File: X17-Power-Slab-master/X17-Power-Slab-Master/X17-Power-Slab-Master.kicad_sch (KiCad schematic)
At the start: 18 parts, among them J2 ET60T-D04-3-08-D04-X-R1-S, J3 796636-6, Q2 IRF1018ESTRLPBF, U1 AZ1117IH-3.3TRG1

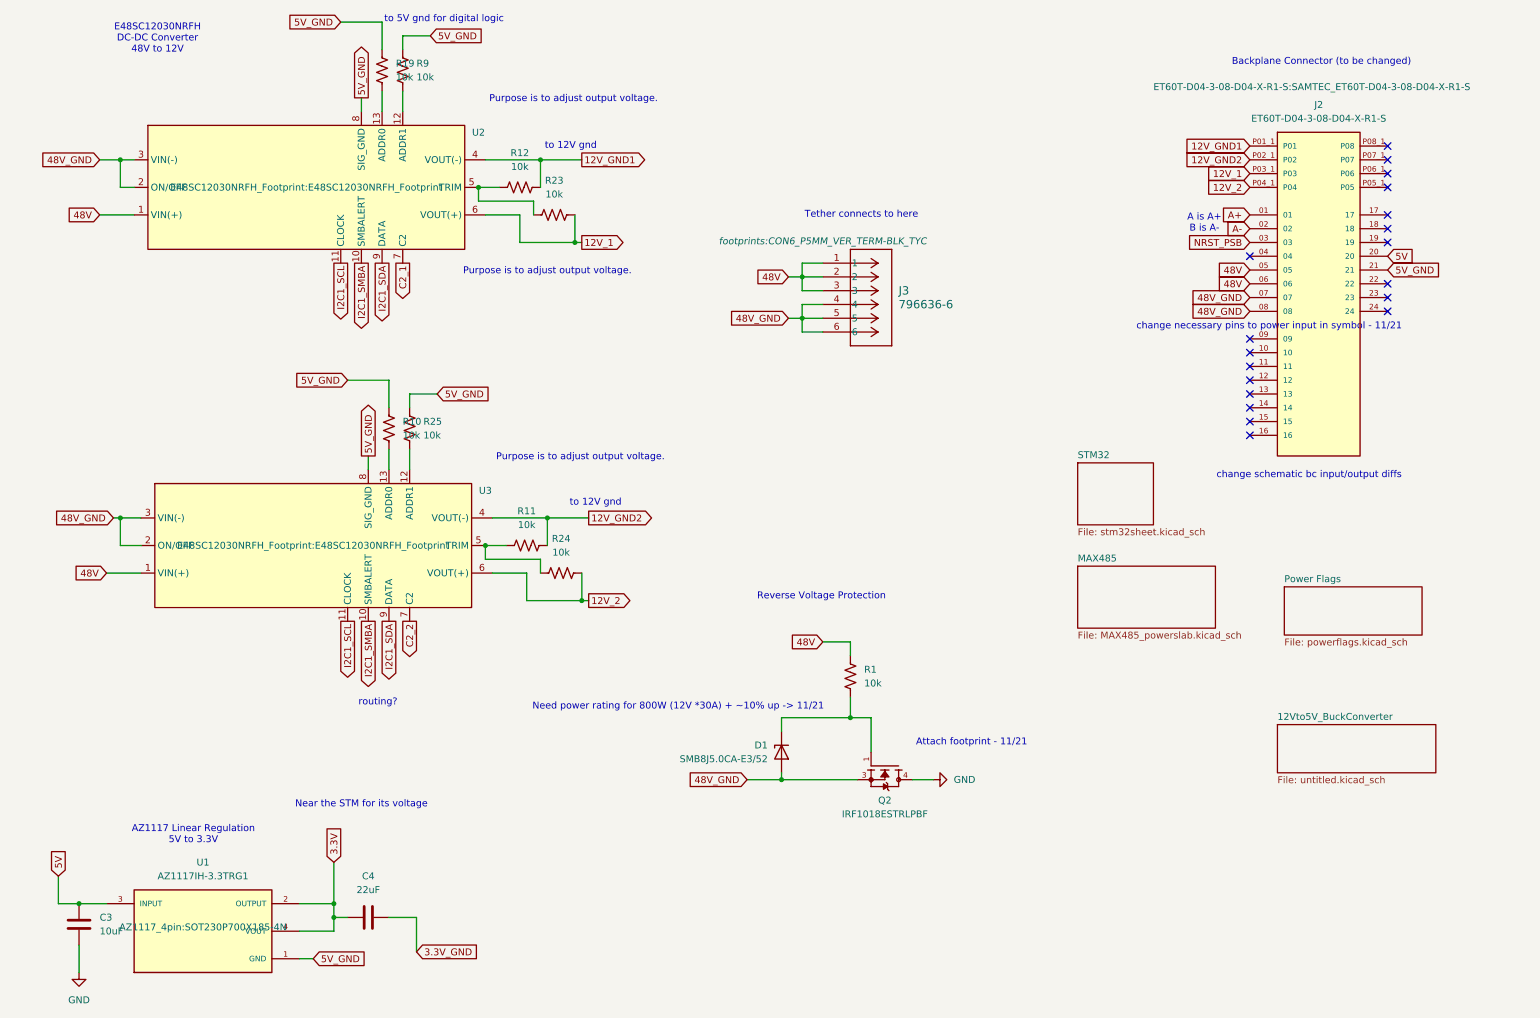
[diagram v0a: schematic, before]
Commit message: Routes
Cannot fill the polygons for some reason
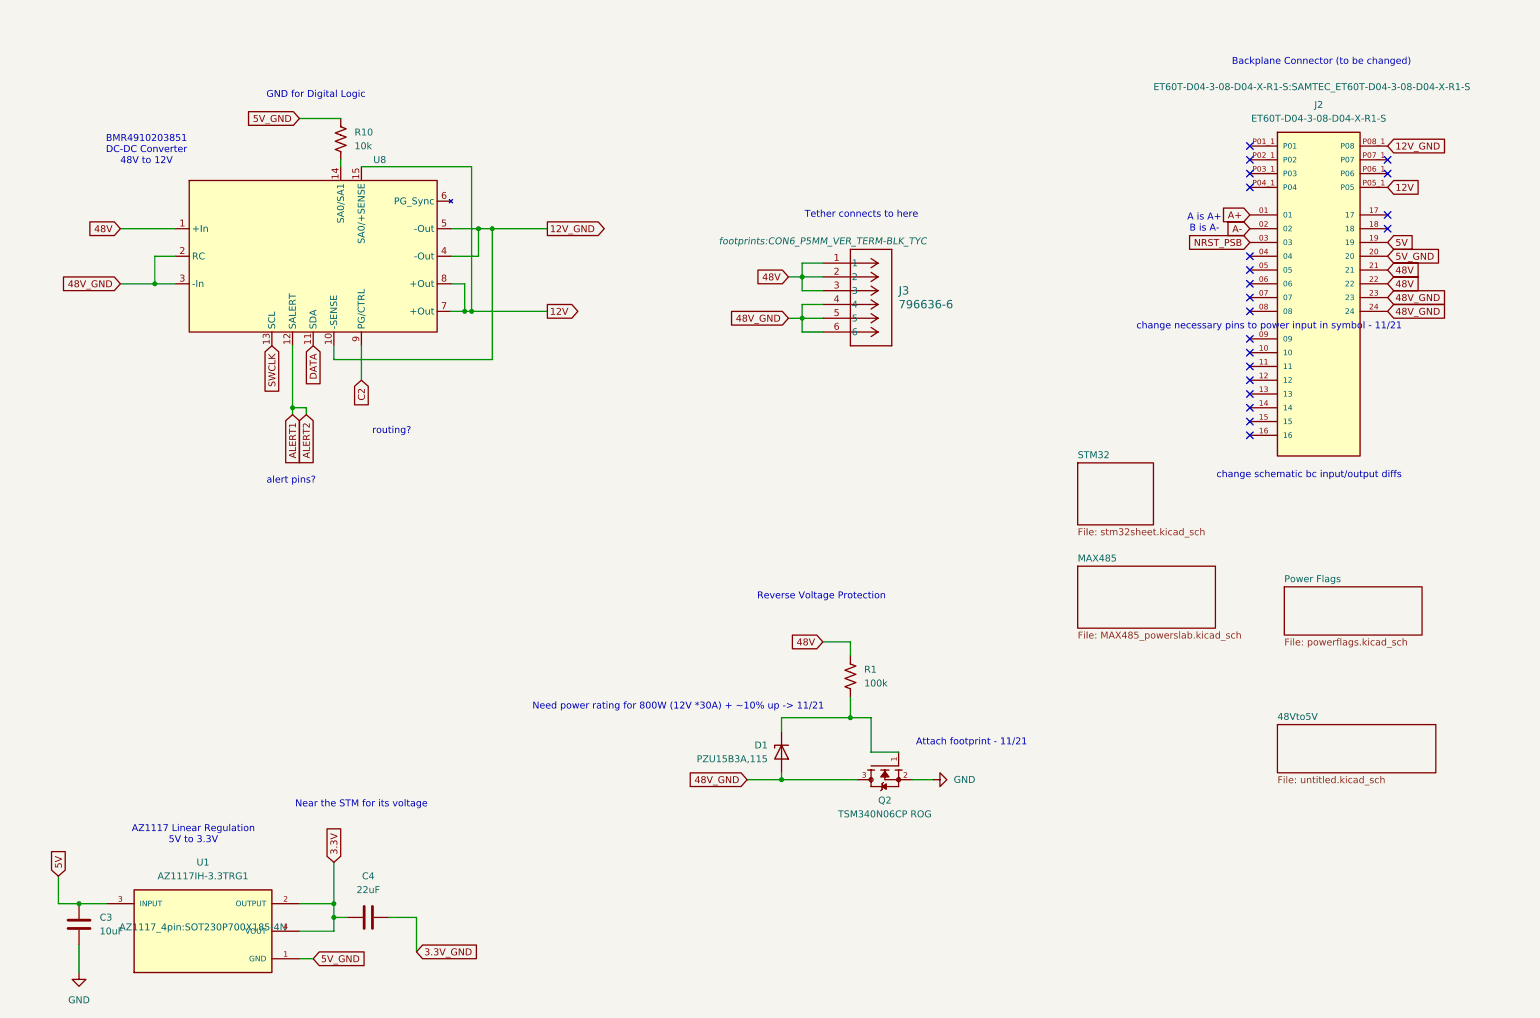
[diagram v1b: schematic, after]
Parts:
- removed R11, R12, R19, R23, R24, R25, R9: 10k, Resistor_SMD:R_0603_1608Metric_Pad0.98x0.95mm_HandSolder, symbol Device:R_US
- removed U2, U3: ~, E48SC12030NRFH_Footprint:E48SC12030NRFH_Footprint, symbol E48SC12030NRFH_New:E48SC12030NRFH
- added U8: ~, BMR491_MadeByMe:BMR4910203851, symbol BMR491_SymbolByMe:BMR4910203/851
- D1: value SMB8J5.0CA-E3/52 -> PZU15B3A,115
- Q2: value IRF1018ESTRLPBF -> TSM340N06CP ROG; footprint Reverse Voltage Protection:TO254P1524X483-4 -> Reverse Voltage Protection:TRANS_TSM340N06CPROG; MANUFACTURER Infineon -> TSM
- R1: value 10k -> 100k
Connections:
- net 48V: now also J2.21, J2.22, U8.1 (+In); no longer J2.05, J2.06
- net 48V_GND: now also J2.23, J2.24, U8.2 (RC), U8.3 (-In); no longer J2.07, J2.08
- net 5V: now also J2.19; no longer J2.20
- net 5V_GND: now also J2.20; no longer J2.21
- net GND: now also Q2.2; no longer Q2.4
- net at R10.2: now also U8.14 (SA0/SA1)
- net 12V: now reaches J2.P05_1 (P05)
- net 12V: now also U8.15 (SA0/+SENSE), U8.7 (+Out), U8.8 (+Out)
- net 12V_GND: now reaches J2.P08_1 (P08)
- net 12V_GND: now also U8.10 (-SENSE), U8.4 (-Out), U8.5 (-Out)
- net 12V_1: no longer names the net of J2.P03_1 (P03)
- net 12V_2: no longer names the net of J2.P04_1 (P04)
- net 12V_GND1: no longer names the net of J2.P01_1 (P01)
- net 12V_GND2: no longer names the net of J2.P02_1 (P02)
- new net ALERT1: U8.12 (SALERT)
- new net C2: U8.9 (PG/CTRL)
- new net DATA: U8.11 (SDA)
- new net SWCLK: U8.13 (SCL)
- no-connect marks 19 -> 21
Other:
- sheet 12Vto5V_BuckConverter renamed 48Vto5V
- note added: "BMR4910203851 DC-DC Converter 48V to 12V"
- note added: "GND for Digital Logic"
- note added: "alert pins?"
- note removed: "E48SC12030NRFH DC-DC Converter 48V to 12V"
- note removed: "Purpose is to adjust output voltage."
- note removed: "to 12V gnd"
- note removed: "to 5V gnd for digital logic"
- moved on the sheet: Q2

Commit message: Power traces update
I think I'm getting the idea of power traces needed?
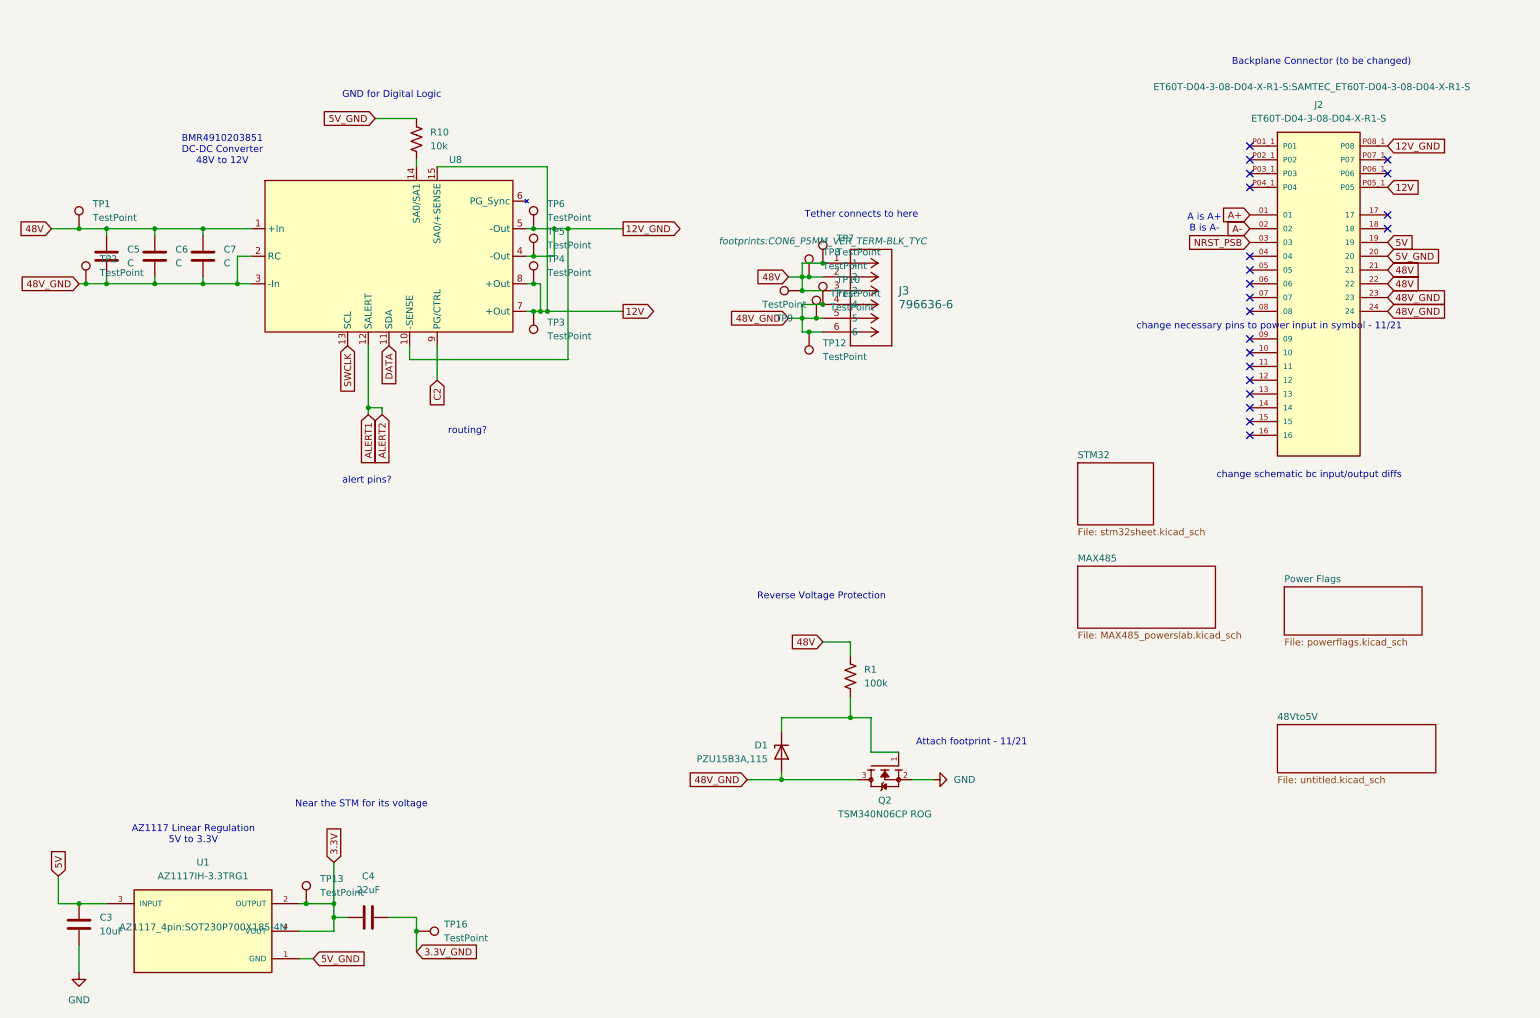
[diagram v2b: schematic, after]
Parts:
- added C5, C6, C7: C, Brick Decoupling Capacitors:CAP_50TPV_10x10.5_RBY, symbol Device:C
- added TP1, TP10, TP11, TP12, TP13, TP16, TP2, TP3, TP4, TP5, TP6, TP7, TP8, TP9: TestPoint, TestPoint:TestPoint_Pad_D4.0mm, symbol Connector:TestPoint
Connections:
- net 12V: now also TP3.1, TP4.1
- net 12V_GND: now also TP5.1, TP6.1
- net 3.3V: now also TP13.1
- net 3.3V_GND: now also TP16.1
- net 48V: now also C5.1, C6.1, C7.1, TP1.1, TP7.1, TP8.1, TP9.1
- net 48V_GND: now also C5.2, C6.2, C7.2, TP10.1, TP11.1, TP12.1, TP2.1
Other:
- note removed: "Need power rating for 800W (12V *30A) + ~10% up -> 11/21"
- moved on the sheet: R10, U8

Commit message: Change to combined 12V 5V gnd
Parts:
- removed TP10, TP11, TP12, TP7, TP8, TP9: TestPoint, TestPoint:TestPoint_Pad_D4.0mm, symbol Connector:TestPoint
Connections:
- net 5V_GND is gone; now on net 12V_5V_GND: J2.20, R10.1, U1.1 (GND)
- net 12V: no longer TP4.1
- net 48V: now also TP5.1
- net 48V_GND: no longer J3.4, J3.5, J3.6
- net A+: now also J2.02; no longer J2.01
- net A-: now also J2.01; no longer J2.02
- net GND: no longer Q2.2
- net 12V_GND renamed 12V_5V_GND
- net 12V_5V_GND: now also TP4.1; no longer TP5.1, TP6.1
- new net RAW_48V_GND: J3.4, J3.5, J3.6, Q2.2, TP6.1
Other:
- note added: "B is A- A is A+"
- note removed: "A is A+ B is A-"

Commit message: Connector pins renamed and attempt @ fixing airwires for 5V Brick
Still don't understand why the airwire from 5V to 12V_5V_GND test point exists, I also now have airwires across all my P08_1 pins despite the same set up existing for 12V.
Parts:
- D1: footprint Diode_SMD:D_1210_3225Metric_Pad1.42x2.65mm_HandSolder -> Diode_SMD:D_MiniMELF
- J2: footprint ET60T-D04-3-08-D04-X-R1-S:SAMTEC_ET60T-D04-3-08-D04-X-R1-S -> ET60S-D04-3-08-D04-X-R1-S:SAMTEC_ET60S-D04-3-08-D04-X-R1-S
- J3: footprint footprints:CON6_P5MM_VER_TERM-BLK_TYC -> CON6_P5MM_VER_TERM-BLK_TYC
- U1: footprint AZ1117_4pin:SOT230P700X185-4N -> AZ1117IH-3.3TRG1:SOT230P700X185-4N
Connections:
- net 12V_5V_GND: no longer U1.1 (GND)
- no-connect marks 21 -> 22
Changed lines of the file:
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@@
+	)
+	(no_connect
+		(at 67.31 187.96)
 	)
 	(no_connect
@@
 				)
 				(justify right)
-				(hide yes)
-			)
-		)
-	)
-	(global_label "12V_5V_GND"
-		(shape input)
-		(at 67.31 187.96 0)
-		(fields_autoplaced yes)
-		(effects
-			(font
-				(size 1.27 1.27)
-			)
-			(justify left)
-		)
-		(property "Intersheetrefs" "${INTERSHEET_REFS}"
-			(at 81.9066 187.96 0)
-			(effects
-				(font
-					(size 1.27 1.27)
-				)
-				(justify left)
 				(hide yes)
 			)
@@
 			)
 		)
-		(property "Footprint" "ET60T-D04-3-08-D04-X-R1-S:SAMTEC_ET60T-D04-3-08-D04-X-R1-S"
+		(property "Footprint" "ET60S-D04-3-08-D04-X-R1-S:SAMTEC_ET60S-D04-3-08-D04-X-R1-S"
 			(at 251.46 27.94 0)
 			(effects
@@
 			)
 		)
-		(property "Footprint" "footprints:CON6_P5MM_VER_TERM-BLK_TYC"
+		(property "Footprint" "CON6_P5MM_VER_TERM-BLK_TYC"
 			(at 161.29 55.626 0)
 			(effects
@@
 			)
 		)
-		(property "Description" "Decoupling Capacitor for the Brick"
+		(property "Description" "Unpolarized capacitor"
 			(at 29.21 58.42 0)
 			(effects
@@
 			)
 		)
-		(property "Footprint" "Diode_SMD:D_1210_3225Metric_Pad1.42x2.65mm_HandSolder"
+		(property "Footprint" "Diode_SMD:D_MiniMELF"
 			(at 158.115 149.86 0)
 			(effects
@@
 			)
 		)
-		(property "Datasheet" "https://assets.nexperia.com/documents/data-sheet/PZUXBA_SER.pdf"
+		(property "Datasheet" "https://assets.nexperia.com/documents/data-sheet/BZV55_SER.pdf"
 			(at 153.67 149.86 0)
 			(effects
@@
 			)
 		)
-		(property "Description" "Decoupling Capacitor for the Brick"
+		(property "Description" "Unpolarized capacitor"
 			(at 46.99 58.42 0)
 			(effects
@@
 			)
 		)
-		(property "Description" "Decoupling Capacitor for the Brick"
+		(property "Description" "Unpolarized capacitor"
 			(at 38.1 58.42 0)
 			(effects
@@
 			)
 		)
-		(property "Footprint" "AZ1117_4pin:SOT230P700X185-4N"
+		(property "Footprint" "AZ1117IH-3.3TRG1:SOT230P700X185-4N"
 			(at 46.99 182.88 0)
 			(effects

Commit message: Minor Edits
Some layout edits, got rid of stm, not done yet
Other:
- removed sheet MAX485
- removed sheet STM32
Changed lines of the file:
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@@
-	)
-	(sheet
-		(at 208.28 96.52)
-		(size 13.97 11.43)
-		(fields_autoplaced yes)
-		(stroke
-			(width 0.1524)
-			(type solid)
-		)
-		(fill
-			(color 0 0 0 0.0000)
-		)
-		(property "Sheetname" "STM32"
-			(at 208.28 95.8084 0)
-			(effects
-				(font
-					(size 1.27 1.27)
-				)
-				(justify left bottom)
-			)
-		)
-		(property "Sheetfile" "stm32sheet.kicad_sch"
-			(at 208.28 108.5346 0)
-			(effects
-				(font
-					(size 1.27 1.27)
-				)
-				(justify left top)
-			)
-		)
-		(instances
-			(project "X17-Power-Slab-Master"
-				(path "/57e59c68-7be1-495e-b535-e78e0f561e15"
-					(page "6")
-				)
-			)
-		)
-	)
-	(sheet
-		(at 208.28 115.57)
-		(size 25.4 11.43)
-		(fields_autoplaced yes)
-		(stroke
-			(width 0.1524)
-			(type solid)
-		)
-		(fill
-			(color 0 0 0 0.0000)
-		)
-		(property "Sheetname" "MAX485"
-			(at 208.28 114.8584 0)
-			(effects
-				(font
-					(size 1.27 1.27)
-				)
-				(justify left bottom)
-			)
-		)
-		(property "Sheetfile" "MAX485_powerslab.kicad_sch"
-			(at 208.28 127.5846 0)
-			(effects
-				(font
-					(size 1.27 1.27)
-				)
-				(justify left top)
-			)
-		)
-		(instances
-			(project "X17-Power-Slab-Master"
-				(path "/57e59c68-7be1-495e-b535-e78e0f561e15"
-					(page "4")
-				)
-			)
-		)
 	)
 	(sheet

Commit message: final for 12/30 meeting
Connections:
- net 12V_5V_GND: now also J2.12
- net 48V: now also J2.13, J2.14
- net 48V_GND: now also J2.08, J2.16; no longer J2.23
- no-connect marks 22 -> 18
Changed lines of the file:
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@@
-	)
-	(no_connect
-		(at 240.03 81.28)
 	)
 	(no_connect
@@
 	)
 	(no_connect
+		(at 265.43 66.04)
+	)
+	(no_connect
 		(at 240.03 76.2)
 	)
@@
 	)
 	(no_connect
+		(at 67.31 187.96)
+	)
+	(no_connect
+		(at 240.03 38.1)
+	)
+	(no_connect
+		(at 240.03 45.72)
+	)
+	(no_connect
+		(at 265.43 53.34)
+	)
+	(no_connect
+		(at 240.03 60.96)
+	)
+	(no_connect
+		(at 265.43 43.18)
+	)
+	(no_connect
+		(at 240.03 88.9)
+	)
+	(no_connect
+		(at 240.03 58.42)
+	)
+	(no_connect
+		(at 265.43 50.8)
+	)
+	(no_connect
 		(at 240.03 63.5)
-	)
-	(no_connect
-		(at 67.31 187.96)
-	)
-	(no_connect
-		(at 240.03 38.1)
-	)
-	(no_connect
-		(at 240.03 45.72)
-	)
-	(no_connect
-		(at 265.43 53.34)
-	)
-	(no_connect
-		(at 240.03 60.96)
-	)
-	(no_connect
-		(at 265.43 43.18)
-	)
-	(no_connect
-		(at 240.03 88.9)
-	)
-	(no_connect
-		(at 240.03 58.42)
-	)
-	(no_connect
-		(at 240.03 68.58)
-	)
-	(no_connect
-		(at 265.43 50.8)
-	)
-	(no_connect
-		(at 240.03 86.36)
-	)
-	(no_connect
-		(at 240.03 91.44)
-	)
-	(no_connect
-		(at 240.03 83.82)
 	)
 	(no_connect
@@
 		)
 	)
+	(global_label "48V_GND"
+		(shape input)
+		(at 240.03 68.58 180)
+		(fields_autoplaced yes)
+		(effects
+			(font
+				(size 1.27 1.27)
+			)
+			(justify right)
+		)
+		(property "Intersheetrefs" "${INTERSHEET_REFS}"
+			(at 228.6991 68.58 0)
+			(effects
+				(font
+					(size 1.27 1.27)
+				)
+				(justify right)
+				(hide yes)
+			)
+		)
+	)
 	(global_label "48V"
 		(shape input)
+		(at 240.03 86.36 180)
+		(fields_autoplaced yes)
+		(effects
+			(font
+				(size 1.27 1.27)
+			)
+			(justify right)
+		)
+		(property "Intersheetrefs" "${INTERSHEET_REFS}"
+			(at 233.5372 86.36 0)
+			(effects
+				(font
+					(size 1.27 1.27)
+				)
+				(justify right)
+				(hide yes)
+			)
+		)
+	)
+	(global_label "48V"
+		(shape input)
 		(at 19.05 53.34 180)
 		(fields_autoplaced yes)
@@
 		)
 	)
+	(global_label "48V_GND"
+		(shape input)
+		(at 240.03 91.44 180)
+		(fields_autoplaced yes)
+		(effects
+			(font
+				(size 1.27 1.27)
+			)
+			(justify right)
+		)
+		(property "Intersheetrefs" "${INTERSHEET_REFS}"
+			(at 228.6991 91.44 0)
+			(effects
+				(font
+					(size 1.27 1.27)
+				)
+				(justify right)
+				(hide yes)
+			)
+		)
+	)
 	(global_label "12V_5V_GND"
 		(shape input)
@@
 		(property "Intersheetrefs" "${INTERSHEET_REFS}"
 			(at 280.0266 58.42 0)
+			(effects
+				(font
+					(size 1.27 1.27)
+				)
+				(justify left)
+				(hide yes)
+			)
+		)
+	)
+	(global_label "48V"
+		(shape input)
+		(at 265.43 60.96 0)
+		(fields_autoplaced yes)
+		(effects
+			(font
+				(size 1.27 1.27)
+			)
+			(justify left)
+		)
+		(property "Intersheetrefs" "${INTERSHEET_REFS}"
+			(at 271.9228 60.96 0)
 			(effects
 				(font
@@
 		)
 	)
+	(global_label "12V_5V_GND"
+		(shape input)
+		(at 240.03 81.28 180)
+		(fields_autoplaced yes)
+		(effects
+			(font
+				(size 1.27 1.27)
+			)
+			(justify right)
+		)
+		(property "Intersheetrefs" "${INTERSHEET_REFS}"
+			(at 225.4334 81.28 0)
+			(effects
+				(font
+					(size 1.27 1.27)
+				)
+				(justify right)
+				(hide yes)
+			)
+		)
+	)
 	(global_label "48V"
 		(shape input)
-		(at 265.43 60.96 0)
-		(fields_autoplaced yes)
-		(effects
-			(font
-				(size 1.27 1.27)
-			)
-			(justify left)
-		)
-		(property "Intersheetrefs" "${INTERSHEET_REFS}"
-			(at 271.9228 60.96 0)
-			(effects
-				(font
-					(size 1.27 1.27)
-				)
-				(justify left)
-				(hide yes)
-			)
-		)
-	)
-	(global_label "48V_GND"
-		(shape input)
-		(at 265.43 66.04 0)
-		(fields_autoplaced yes)
-		(effects
-			(font
-				(size 1.27 1.27)
-			)
-			(justify left)
-		)
-		(property "Intersheetrefs" "${INTERSHEET_REFS}"
-			(at 276.7609 66.04 0)
-			(effects
-				(font
-					(size 1.27 1.27)
-				)
-				(justify left)
-				(hide yes)
-			)
+		(at 240.03 83.82 180)
+		(fields_autoplaced yes)
+		(effects
+			(font
+				(size 1.27 1.27)
+			)
+			(justify right)
+		)
+		(property "Intersheetrefs" "${INTERSHEET_REFS}"
+			(at 233.5372 83.82 0)
+			(effects
+				(font
+					(size 1.27 1.27)
+				)
+				(justify right)
+				(hide yes)
+			)

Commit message: changes 1/3/25
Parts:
- removed C3: 10uF, Capacitor_SMD:C_0603_1608Metric_Pad1.08x0.95mm_HandSolder, symbol Device:C
- removed C4: 22uF, Capacitor_SMD:C_0603_1608Metric_Pad1.08x0.95mm_HandSolder, symbol Device:C
- removed TP1, TP13, TP16, TP4: TestPoint, TestPoint:TestPoint_Pad_D4.0mm, symbol Connector:TestPoint
- removed U1: AZ1117IH-3.3TRG1, AZ1117IH-3.3TRG1:SOT230P700X185-4N, symbol AZ1117H 4pin:AZ1117IH-3.3TRG1
- added J1: Conn_01x12_Pin, DataConv Connector:Data Conversion two 1x6, symbol Connector:Conn_01x12_Pin
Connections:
- net 12V_5V_GND: now also J1.1 (Pin_1), J1.8 (Pin_8)
- net 5V: now also J1.7 (Pin_7)
- net A+: now also J1.11 (Pin_11)
- net A-: now also J1.12 (Pin_12)
- net ALERT1: now also J1.5 (Pin_5)
- net DATA: now also J1.2 (Pin_2)
- net NRST_PSB: now also J1.10 (Pin_10)
- net SWCLK: now also J1.9 (Pin_9)
- net C2 renamed PG
- net PG: now also J1.6 (Pin_6)
- no-connect marks 18 -> 19
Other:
- note removed: "AZ1117 Linear Regulation 5V to 3.3V"
- note removed: "Attach footprint - 11/21"
- note removed: "Near the STM for its voltage"
- moved on the sheet: D1, Q2, R1
